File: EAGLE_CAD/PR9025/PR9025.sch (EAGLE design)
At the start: 66 parts, among them SW1 C&K_PTS645, U1 SI4702-C19-GMR, X1 ABS25XTAL

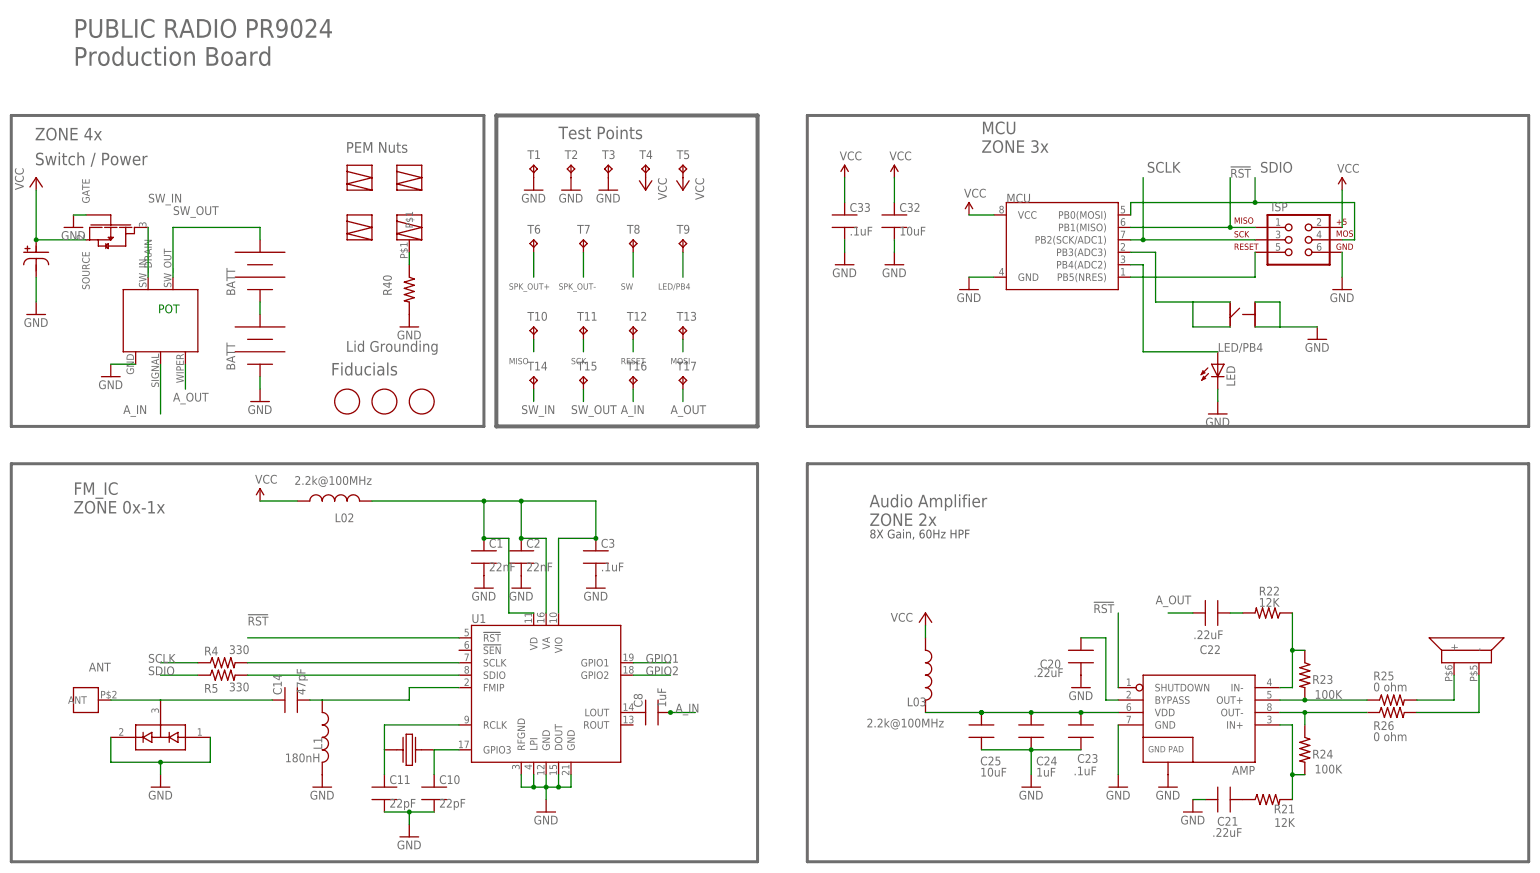
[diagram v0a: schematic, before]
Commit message: PR9025
Updated DFM rework from Josh
- removed R4 & R5
- FM_IC Sen tied high

Simplified board dimension outline
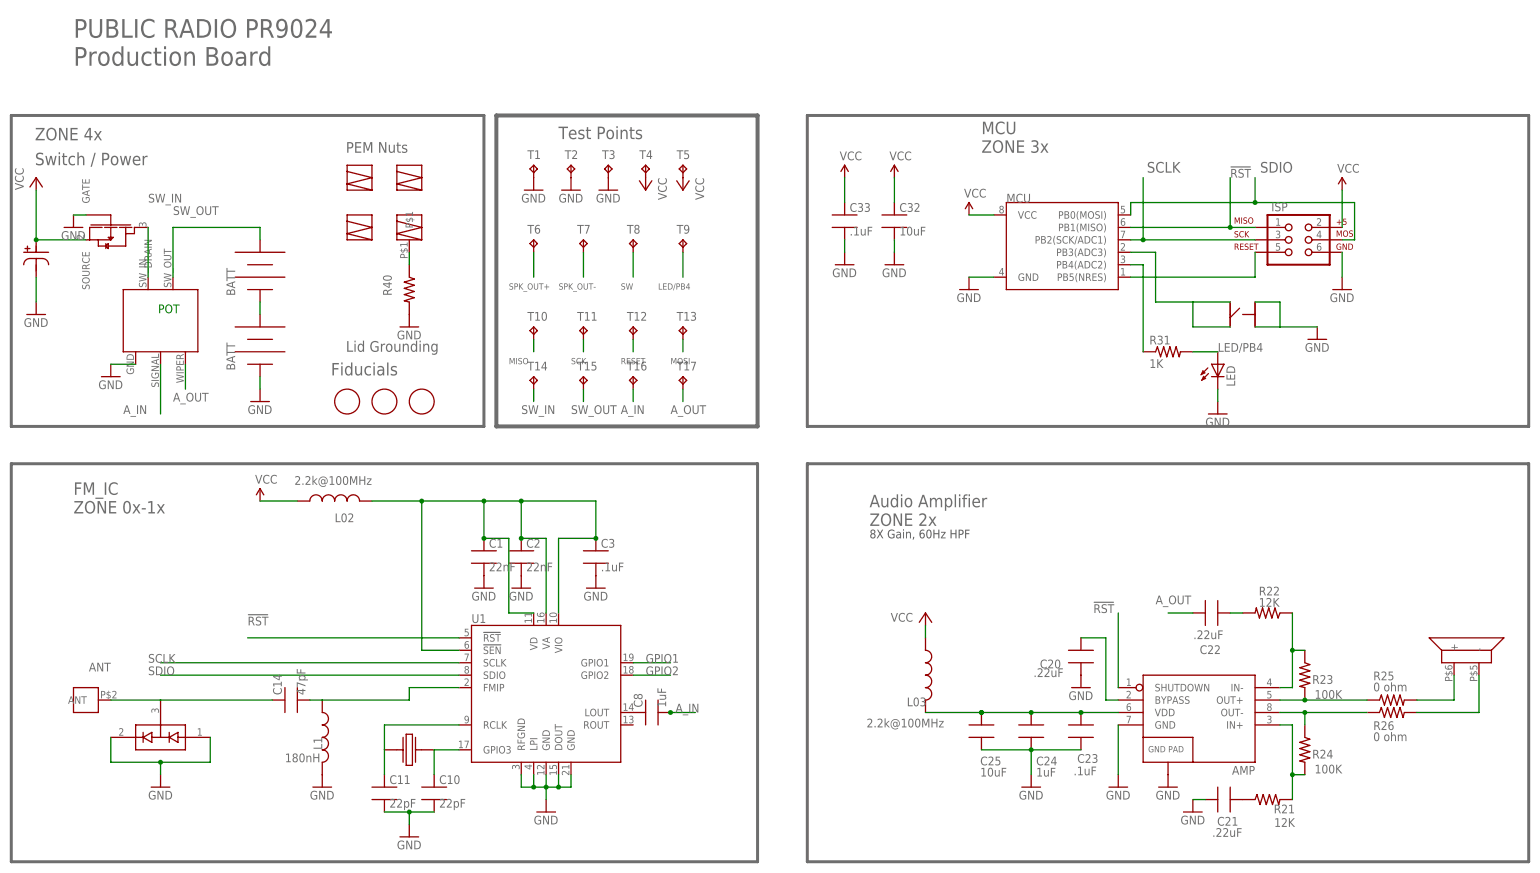
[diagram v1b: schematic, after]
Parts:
- removed R4, R5: 330, PR_Parts_Library:R_SMT_R0603_CPL
- added R31: 1K, PR_Parts_Library:R_SMT_R0603_CPL
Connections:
- removed net SCLK-L: R4.2, U1.SCLK
- removed net SDIO-L: R5.2, U1.SDIO
- new net N$7: LED.A, R31.2
- net 3.3V: now also U1.!SEN
- net LED/PB4: now also R31.1; no longer LED.A
- net SCLK: now also U1.SCLK; no longer R4.1
- net SDIO: now also U1.SDIO; no longer R5.1
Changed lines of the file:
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@@
 <attribute name="VOLTAGE" value="16V"/>
-</part>
-<part name="R4" library="PR_Parts_Library" deviceset="R_SMT" device="_R0603_CPL" value="330">
-<attribute name="MFG_PN" value="MCR03ERTJ331"/>
-<attribute name="POWER" value="1/10W"/>
-<attribute name="TOL" value="5%"/>
-</part>
-<part name="R5" library="PR_Parts_Library" deviceset="R_SMT" device="_R0603_CPL" value="330">
-<attribute name="MFG_PN" value="MCR03ERTJ331"/>
-<attribute name="POWER" value="1/10W"/>
-<attribute name="TOL" value="5%"/>
 </part>
 <part name="C2" library="PR_Parts_Library" deviceset="C_SMT" device="_0603_CPL" value="22nF">
@@
 <part name="U$4" library="PR_Parts_Library" deviceset="PEM_SMT" device=""/>
 <part name="U$5" library="PR_Parts_Library" deviceset="PEM_M3_SMT_W/PIN" device=""/>
+<part name="R31" library="PR_Parts_Library" deviceset="R_SMT" device="_R0603_CPL" value="1K">
+<attribute name="MFG_PN" value="311-1.00KHRCT-ND"/>
+</part>
 </parts>
 <sheets>
@@
 <instance part="C1" gate="G$1" x="55.88" y="63.5"/>
 <instance part="C3" gate="G$1" x="78.74" y="63.5"/>
-<instance part="R4" gate="G$1" x="2.54" y="40.64" smashed="yes">
-<attribute name="NAME" x="-1.27" y="42.1386" size="1.778" layer="95"/>
-<attribute name="VALUE" x="3.81" y="42.418" size="1.778" layer="96"/>
-</instance>
-<instance part="R5" gate="G$1" x="2.54" y="38.1" smashed="yes">
-<attribute name="NAME" x="-1.27" y="34.5186" size="1.778" layer="95"/>
-<attribute name="VALUE" x="3.81" y="34.798" size="1.778" layer="96"/>
-</instance>
 <instance part="C2" gate="G$1" x="63.5" y="63.5"/>
 <instance part="SW1" gate="G$1" x="210.82" y="111.76" rot="R270"/>
@@
 <instance part="U$4" gate="G$1" x="30.48" y="129.54"/>
 <instance part="U$5" gate="G$1" x="40.64" y="129.54"/>
+<instance part="R31" gate="G$1" x="195.58" y="104.14"/>
 </instances>
 <busses>
@@
 </segment>
 </net>
-<net name="SCLK-L" class="0">
-<segment>
-<wire x1="50.8" y1="40.64" x2="7.62" y2="40.64" width="0.1524" layer="91"/>
-<pinref part="U1" gate="G$1" pin="SCLK"/>
-<pinref part="R4" gate="G$1" pin="2"/>
-</segment>
-</net>
-<net name="SDIO-L" class="0">
-<segment>
-<wire x1="50.8" y1="38.1" x2="7.62" y2="38.1" width="0.1524" layer="91"/>
-<pinref part="U1" gate="G$1" pin="SDIO"/>
-<pinref part="R5" gate="G$1" pin="2"/>
-</segment>
-</net>
 <net name="!RST" class="0">
 <segment>
@@
 <net name="SCLK" class="0">
 <segment>
-<wire x1="-2.54" y1="40.64" x2="-10.16" y2="40.64" width="0.1524" layer="91"/>
 <label x="-12.7" y="40.64" size="1.778" layer="95"/>
-<pinref part="R4" gate="G$1" pin="1"/>
+<wire x1="50.8" y1="40.64" x2="-10.16" y2="40.64" width="0.1524" layer="91"/>
+<pinref part="U1" gate="G$1" pin="SCLK"/>
 </segment>
 <segment>
@@
 <net name="SDIO" class="0">
 <segment>
-<wire x1="-2.54" y1="38.1" x2="-10.16" y2="38.1" width="0.1524" layer="91"/>
 <label x="-12.7" y="38.1" size="1.778" layer="95"/>
-<pinref part="R5" gate="G$1" pin="1"/>
+<wire x1="50.8" y1="38.1" x2="-10.16" y2="38.1" width="0.1524" layer="91"/>
+<pinref part="U1" gate="G$1" pin="SDIO"/>
 </segment>
 <segment>
@@
 <segment>
 <pinref part="L02" gate="G$1" pin="2"/>
-<wire x1="55.88" y1="73.66" x2="33.02" y2="73.66" width="0.1524" layer="91"/>
+<wire x1="55.88" y1="73.66" x2="43.18" y2="73.66" width="0.1524" layer="91"/>
 <pinref part="U1" gate="G$1" pin="VD"/>
+<wire x1="43.18" y1="73.66" x2="33.02" y2="73.66" width="0.1524" layer="91"/>
 <wire x1="66.04" y1="50.8" x2="60.96" y2="50.8" width="0.1524" layer="91"/>
 <wire x1="60.96" y1="50.8" x2="60.96" y2="66.04" width="0.1524" layer="91"/>
@@
 <junction x="63.5" y="73.66"/>
 <junction x="78.74" y="66.04"/>
+<pinref part="U1" gate="G$1" pin="!SEN"/>
+<wire x1="50.8" y1="43.18" x2="43.18" y2="43.18" width="0.1524" layer="91"/>
+<wire x1="43.18" y1="43.18" x2="43.18" y2="73.66" width="0.1524" layer="91"/>
+<junction x="43.18" y="73.66"/>
 </segment>
 </net>
@@
 <pinref part="MCU" gate="G$1" pin="PB4(ADC2)"/>
 <label x="205.74" y="104.14" size="1.778" layer="95"/>
-<pinref part="LED" gate="G$1" pin="A"/>
-<wire x1="190.5" y1="104.14" x2="205.74" y2="104.14" width="0.1524" layer="91"/>
+<pinref part="R31" gate="G$1" pin="1"/>
 </segment>
 <segment>
@@
 </segment>
 </net>
+<net name="N$7" class="0">
+<segment>
+<pinref part="LED" gate="G$1" pin="A"/>
+<pinref part="R31" gate="G$1" pin="2"/>
+<wire x1="200.66" y1="104.14" x2="205.74" y2="104.14" width="0.1524" layer="91"/>
+</segment>
+</net>
